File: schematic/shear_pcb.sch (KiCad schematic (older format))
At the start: 1 part

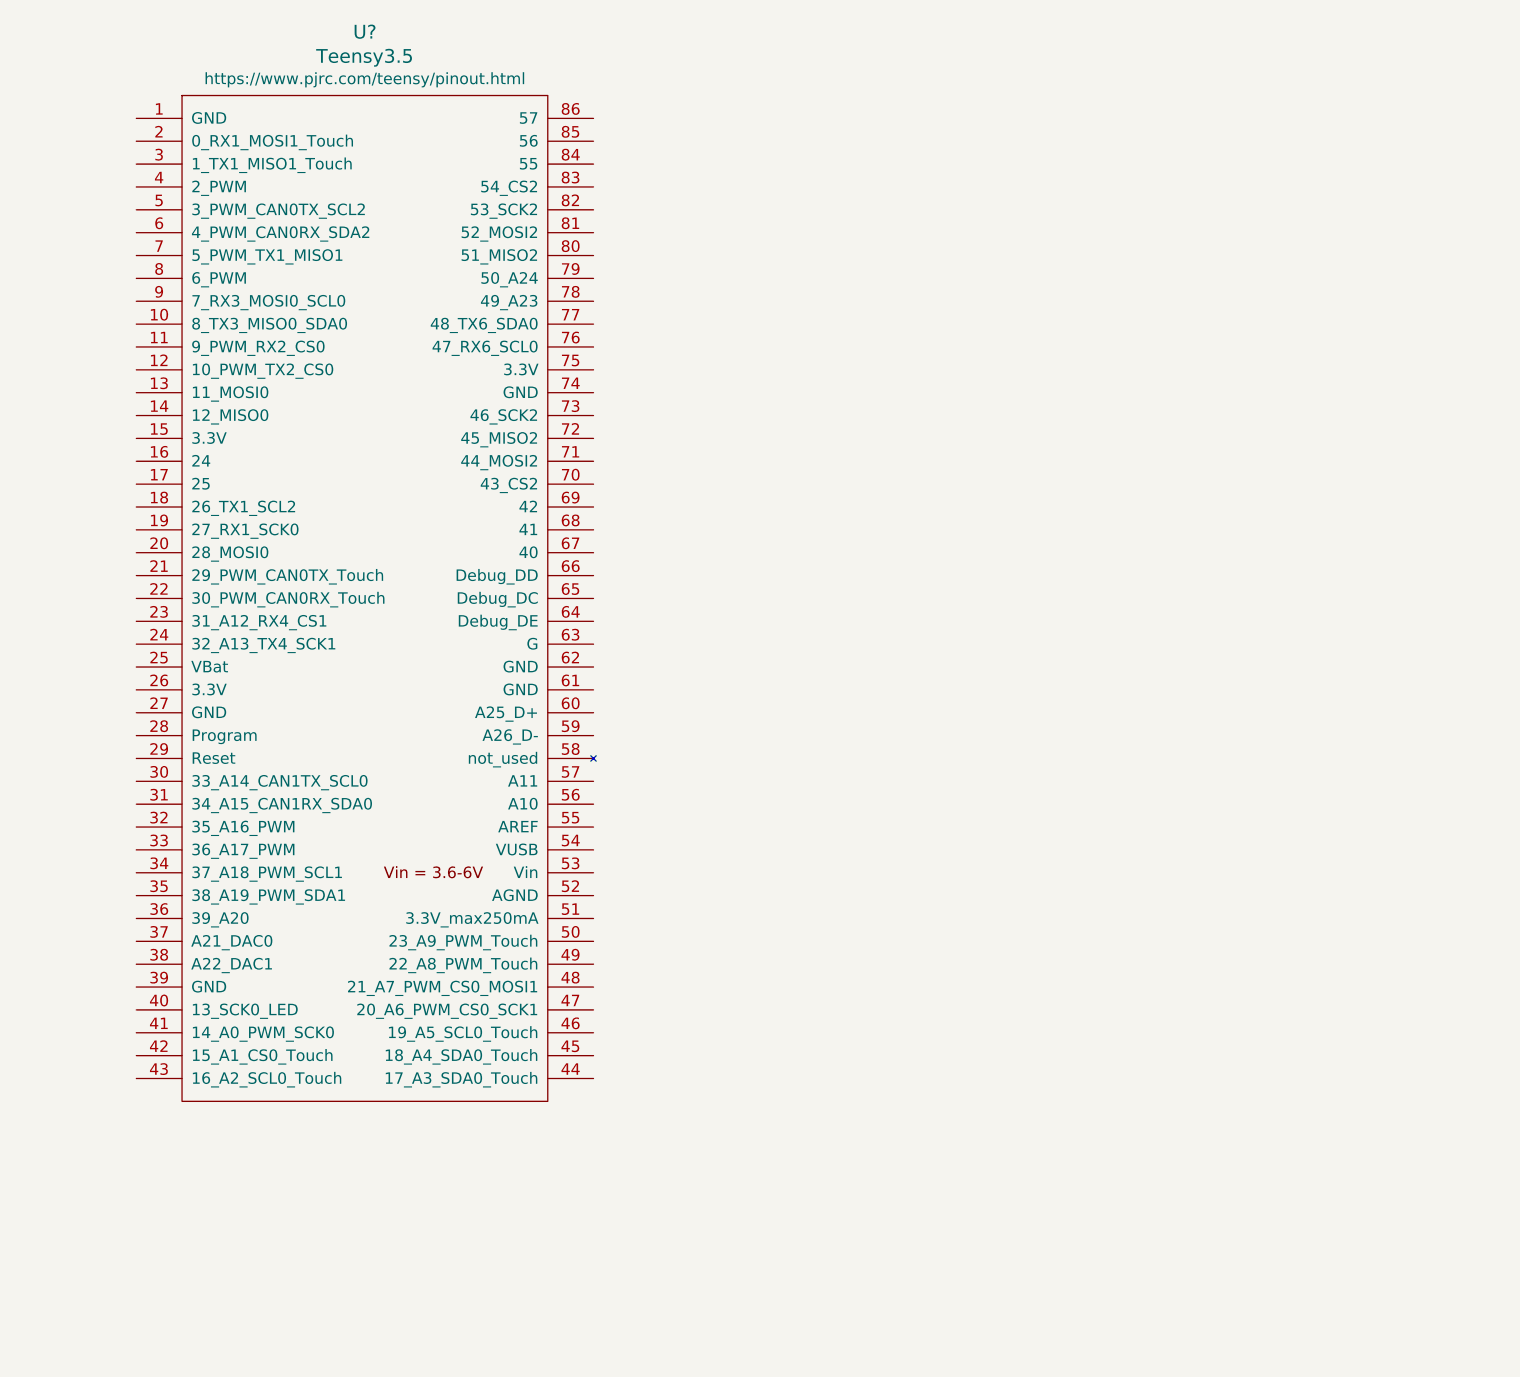
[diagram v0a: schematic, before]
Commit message: Add components to schematic
-2x AMIS30542
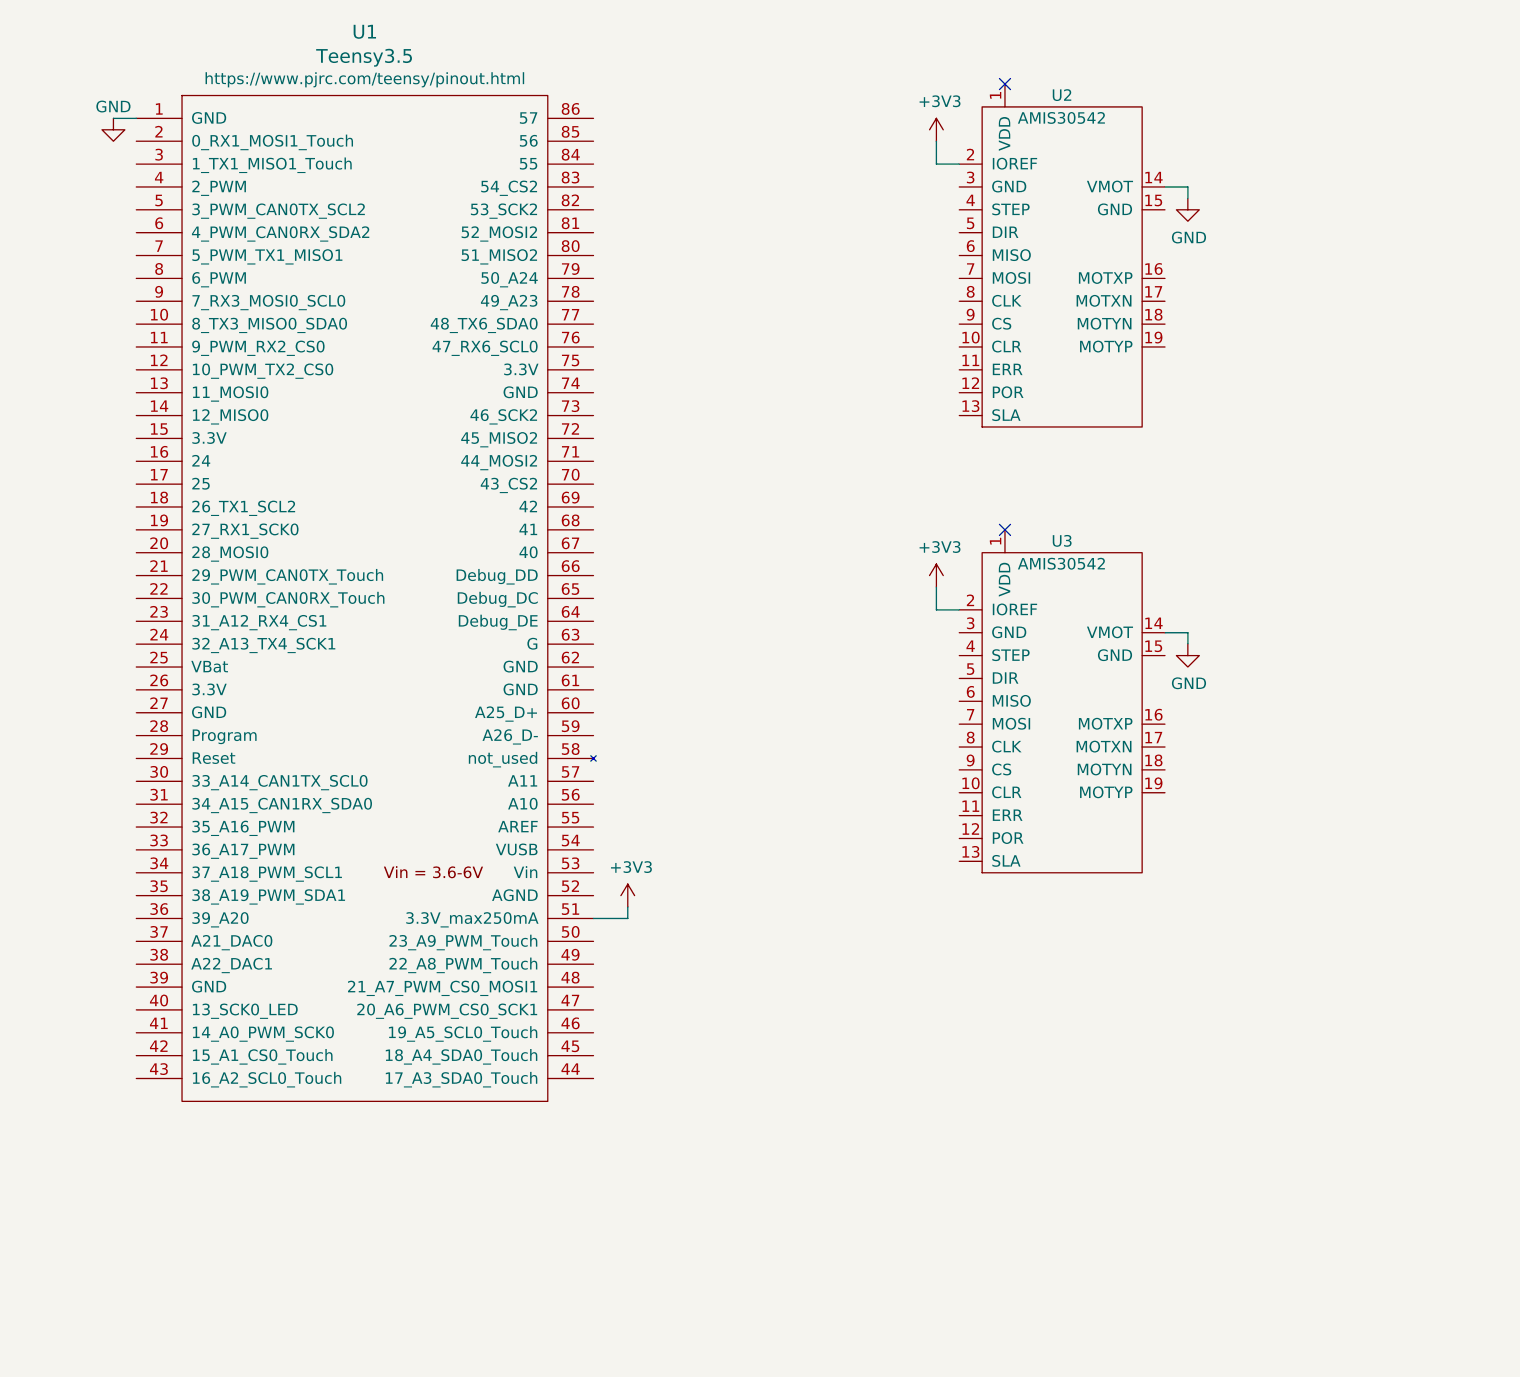
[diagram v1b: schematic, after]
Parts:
- added U2, U3: AMIS30542, AMIS30542:AMIS30542, symbol AMIS30542:AMIS30542
- U1: renamed from U?; footprint (none) -> teensy:Teensy35_36
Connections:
- net GND: now reaches U1.1 (GND)
- net GND: now also U2.14 (VMOT), U3.14 (VMOT)
- net +3V3: now reaches U1.51 (3.3V_max250mA)
- net +3V3: now also U2.2 (IOREF), U3.2 (IOREF)
- no-connect marks 0 -> 2
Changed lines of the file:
@@
 EESchema Schematic File Version 4
+LIBS:shear_pcb-cache
 EELAYER 29 0
 EELAYER END
@@
 $EndDescr
 $Comp
-L teensy:Teensy3.5 U?
+L teensy:Teensy3.5 U1
 U 1 1 5CCA6D74
 P 5600 3150
-F 0 "U?" H 5600 5627 60  0000 C CNN
+F 0 "U1" H 5600 5627 60  0000 C CNN
 F 1 "Teensy3.5" H 5600 5521 60  0000 C CNN
-F 2 "" H 5500 5350 60  0000 C CNN
+F 2 "teensy:Teensy35_36" H 5500 5350 60  0001 C CNN
 F 3 "" H 5600 5450 60  0000 C CNN
 F 4 "https://www.pjrc.com/teensy/pinout.html" H 5600 5423 50  0000 C CNN "Pinouts"
@@
 	1    0    0    -1
 $EndComp
+$Comp
+L AMIS30542:AMIS30542 U3
+U 1 1 5CCD1CB7
+P 8650 3600
+F 0 "U3" H 8650 4300 50  0000 C CNN
+F 1 "AMIS30542" H 8650 4200 50  0000 C CNN
+F 2 "AMIS30542:AMIS30542" H 8650 3800 50  0001 C CNN
+F 3 "" H 8650 3800 50  0001 C CNN
+	1    8650 3600
+	1    0    0    -1
+$EndComp
+NoConn ~ 8400 2850
+NoConn ~ 8400 900
+$Comp
+L AMIS30542:AMIS30542 U2
+U 1 1 5CCCE3DF
+P 8650 1650
+F 0 "U2" H 8650 2350 50  0000 C CNN
+F 1 "AMIS30542" H 8650 2250 50  0000 C CNN
+F 2 "AMIS30542:AMIS30542" H 8650 1850 50  0001 C CNN
+F 3 "" H 8650 1850 50  0001 C CNN
+	1    8650 1650
+	1    0    0    -1
+$EndComp
+$Comp
+L power:+3V3 #PWR0101
+U 1 1 5CCD2832
+P 6750 4500
+F 0 "#PWR0101" H 6750 4350 50  0001 C CNN
+F 1 "+3V3" H 6765 4673 50  0000 C CNN
+F 2 "" H 6750 4500 50  0001 C CNN
+F 3 "" H 6750 4500 50  0001 C CNN
+	1    6750 4500
+	1    0    0    -1
+$EndComp
+$Comp
+L power:+3V3 #PWR0102
+U 1 1 5CCD3EE6
+P 8100 3100
+F 0 "#PWR0102" H 8100 2950 50  0001 C CNN
+F 1 "+3V3" H 8115 3273 50  0000 C CNN
+F 2 "" H 8100 3100 50  0001 C CNN
+F 3 "" H 8100 3100 50  0001 C CNN
+	1    8100 3100
+	1    0    0    -1
+$EndComp
+$Comp
+L power:+3V3 #PWR0103
+U 1 1 5CCD4BBF
+P 8100 1150
+F 0 "#PWR0103" H 8100 1000 50  0001 C CNN
+F 1 "+3V3" H 8115 1323 50  0000 C CNN
+F 2 "" H 8100 1150 50  0001 C CNN
+F 3 "" H 8100 1150 50  0001 C CNN
+	1    8100 1150
+	1    0    0    -1
+$EndComp
+Wire Wire Line
+	8100 1150 8100 1250
+Wire Wire Line
+	8100 1250 8200 1250
+Wire Wire Line
+	8100 3100 8100 3200
+Wire Wire Line
+	8100 3200 8200 3200
+Wire Wire Line
+	6750 4500 6750 4550
+Wire Wire Line
+	6750 4550 6600 4550
+$Comp
+L power:GND #PWR0104
+U 1 1 5CCD61F4
+P 4500 1050
+F 0 "#PWR0104" H 4500 800 50  0001 C CNN
+F 1 "GND" H 4500 1100 50  0000 C CNN
+F 2 "" H 4500 1050 50  0001 C CNN
+F 3 "" H 4500 1050 50  0001 C CNN
+	1    4500 1050
+	1    0    0    -1
+$EndComp
+$Comp
+L power:GND #PWR0105
+U 1 1 5CCD7013
+P 9200 3350
+F 0 "#PWR0105" H 9200 3100 50  0001 C CNN
+F 1 "GND" H 9205 3177 50  0000 C CNN
+F 2 "" H 9200 3350 50  0001 C CNN
+F 3 "" H 9200 3350 50  0001 C CNN
+	1    9200 3350
+	1    0    0    -1
+$EndComp
+$Comp
+L power:GND #PWR0106
+U 1 1 5CCD743D
+P 9200 1400
+F 0 "#PWR0106" H 9200 1150 50  0001 C CNN
+F 1 "GND" H 9205 1227 50  0000 C CNN
+F 2 "" H 9200 1400 50  0001 C CNN
+F 3 "" H 9200 1400 50  0001 C CNN
+	1    9200 1400
+	1    0    0    -1
+$EndComp
+Wire Wire Line
+	9100 3300 9200 3300
+Wire Wire Line
+	9200 3300 9200 3350
+Wire Wire Line
+	9100 1350 9200 1350
+Wire Wire Line
+	9200 1350 9200 1400
+Wire Wire Line
+	4500 1050 4600 1050
 $EndSCHEMATC

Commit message: Connect AMIS drives to Teensy MCU
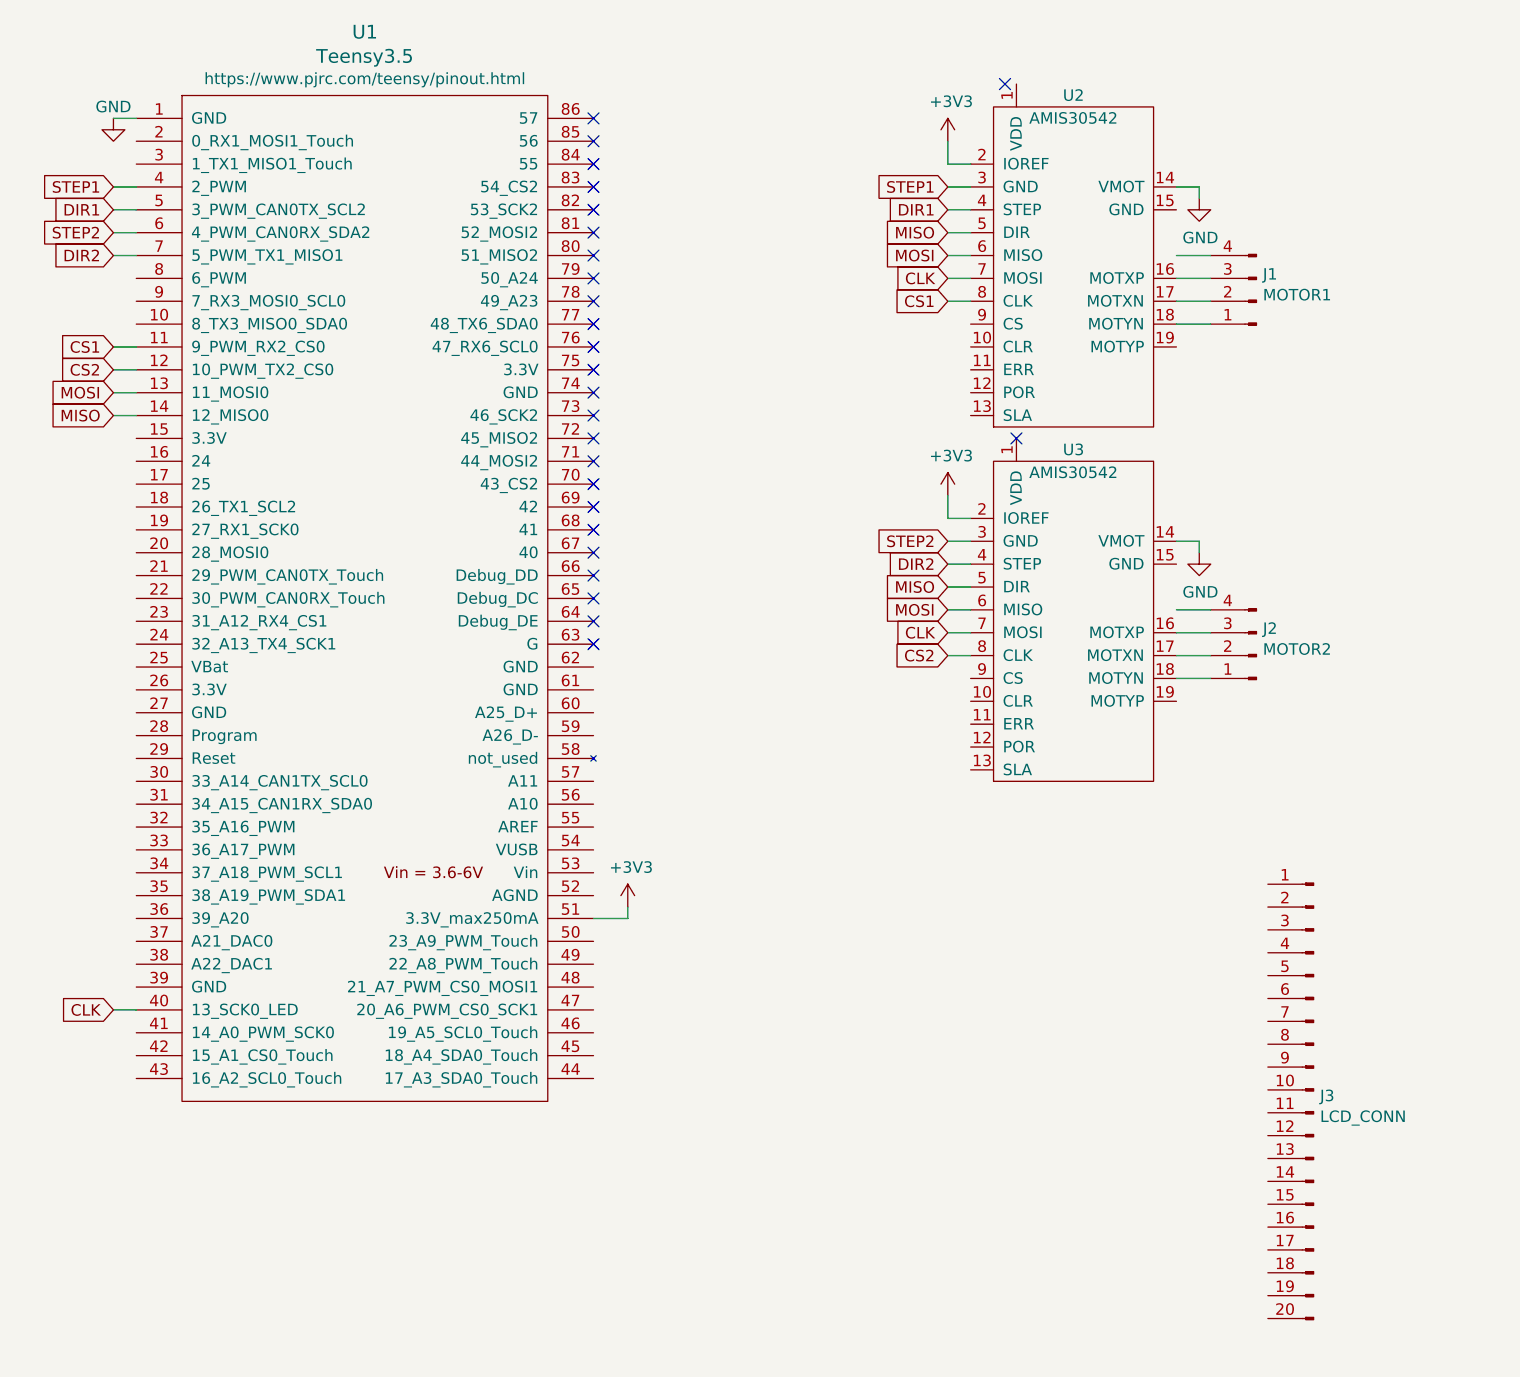
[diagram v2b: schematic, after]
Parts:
- added J1: MOTOR1, Connector_PinHeader_2.54mm:PinHeader_1x04_P2.54mm_Vertical, symbol Connector:Conn_01x04_Male
- added J2: MOTOR2, Connector_PinHeader_2.54mm:PinHeader_1x04_P2.54mm_Vertical, symbol Connector:Conn_01x04_Male
- added J3: LCD_CONN, Connector_PinHeader_2.54mm:PinHeader_1x20_P2.54mm_Vertical, symbol Connector:Conn_01x20_Male
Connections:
- net labels added: CLK, CS1, CS2, DIR1, DIR2, MISO, MOSI, STEP1, STEP2
- wire segments 11 -> 40
- no-connect marks 2 -> 26
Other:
- moved on the sheet: U2, U3
